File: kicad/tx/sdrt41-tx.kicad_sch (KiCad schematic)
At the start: 84 parts, among them J1 I, J2 Q, J3 Conn_01x05_Male, J4 TX, J5 Clock, J6 12V, Q1 2N3904_SOT23, T1 Transformer_1P_SS, U1 LM1117-3.3, U2 MC33078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

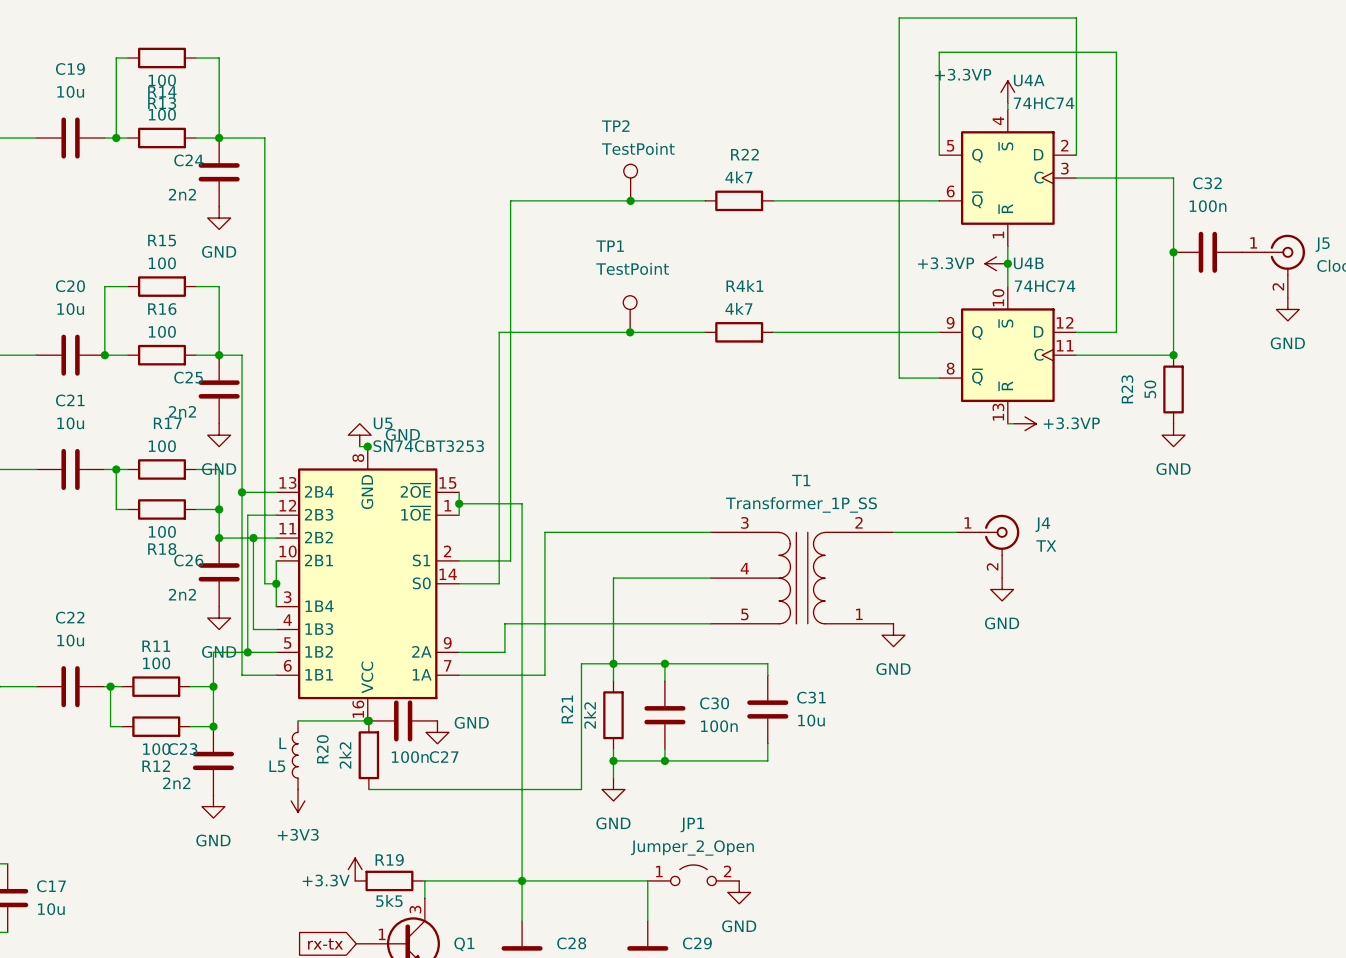
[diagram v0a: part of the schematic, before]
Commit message: Update TX capacitors
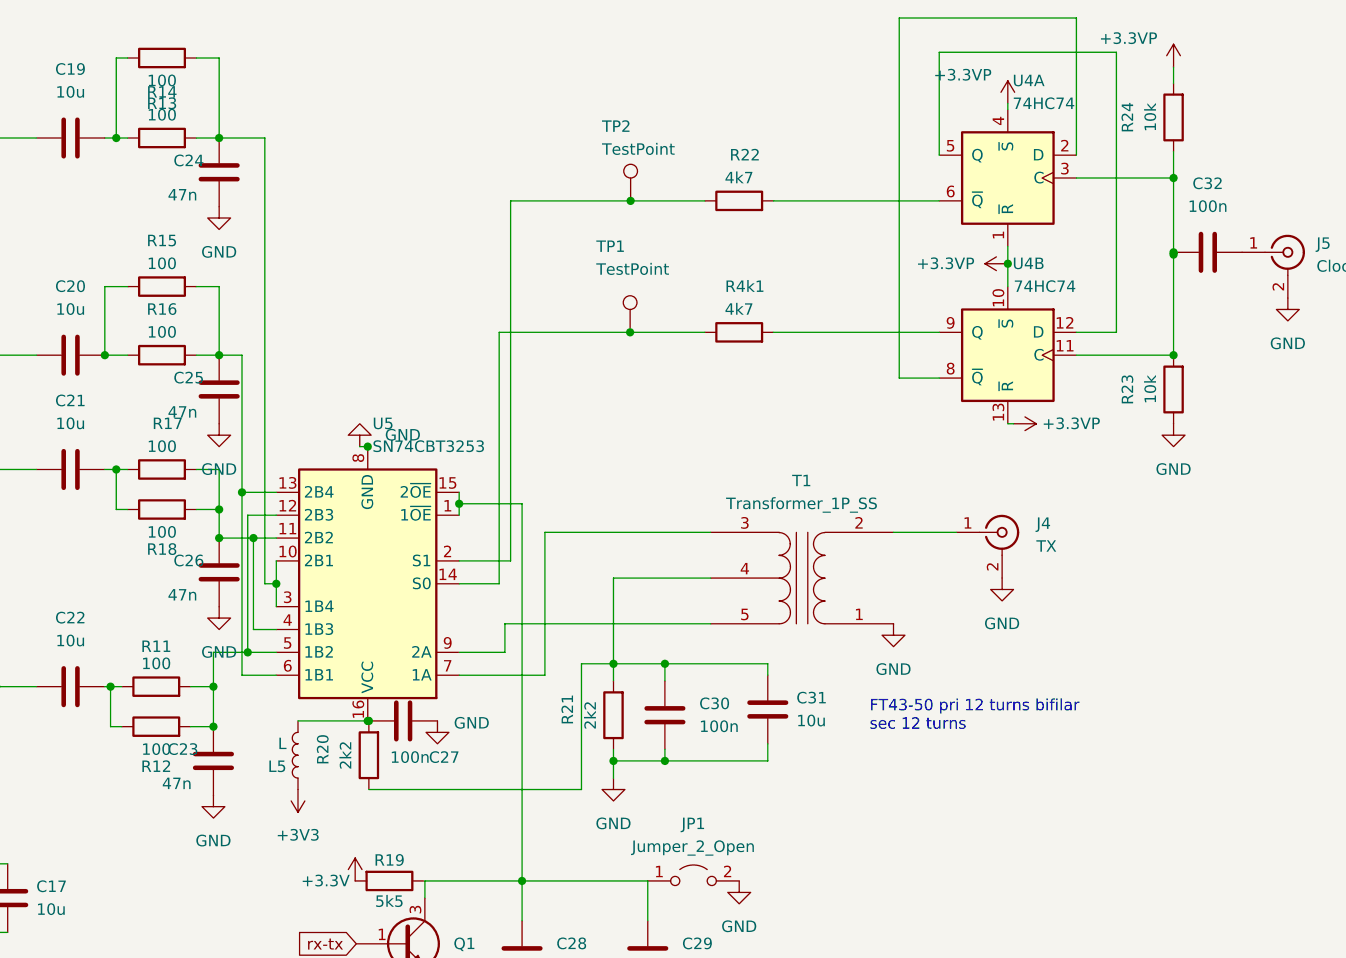
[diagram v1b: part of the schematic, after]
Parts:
- added R24: 10k, Resistor_SMD:R_0805_2012Metric, symbol Device:R
- C23, C24, C25, C26: value 2n2 -> 47n
- R23: value 50 -> 10k
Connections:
- net +3.3VP: now also R24.2
- net at C32.1, R23.2, U4.11 (C)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: now also R24.1
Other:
- note added: "FT43-50 pri 12 turns bifilar sec 12 turns"
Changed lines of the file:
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@@
   (junction (at 73.025 86.995) (diameter 0) (color 0 0 0 0)
   )
+  (junction (at 237.49 49.784) (diameter 0) (color 0 0 0 0)
+  )
   (junction (at 120.015 73.66) (diameter 0) (color 0 0 0 0)
   )
@@
   (junction (at 237.49 60.96) (diameter 0) (color 0 0 0 0)
   )
+  (junction (at 237.49 41.275) (diameter 0) (color 0 0 0 0)
+  )
   (junction (at 73.025 95.25) (diameter 0) (color 0 0 0 0)
   )
@@
     (stroke (width 0) (type default) (color 0 0 0 0))
   )
-  (wire (pts (xy 237.49 49.53) (xy 237.49 60.96))
+  (wire (pts (xy 237.49 49.53) (xy 237.49 49.784))
     (stroke (width 0) (type default) (color 0 0 0 0))
   )
@@
     (stroke (width 0) (type default) (color 0 0 0 0))
   )
+  (wire (pts (xy 237.49 49.784) (xy 237.49 60.96))
+    (stroke (width 0) (type default) (color 0 0 0 0))
+  )
   (wire (pts (xy 180.975 97.155) (xy 180.975 95.25))
     (stroke (width 0) (type default) (color 0 0 0 0))
@@
     (stroke (width 0) (type default) (color 0 0 0 0))
   )
+  (wire (pts (xy 237.49 41.275) (xy 237.49 49.53))
+    (stroke (width 0) (type default) (color 0 0 0 0))
+  )
   (wire (pts (xy 131.445 73.66) (xy 131.445 78.105))
     (stroke (width 0) (type default) (color 0 0 0 0))
@@
     (stroke (width 0) (type default) (color 0 0 0 0))
   )
+  (wire (pts (xy 237.49 30.734) (xy 237.49 28.956))
+    (stroke (width 0) (type default) (color 0 0 0 0))
+  )
   (wire (pts (xy 120.015 73.66) (xy 121.285 73.66))
     (stroke (width 0) (type default) (color 0 0 0 0))
@@
     (stroke (width 0) (type default) (color 0 0 0 0))
   )
-  (wire (pts (xy 237.49 41.275) (xy 237.49 49.53))
+  (wire (pts (xy 237.49 38.354) (xy 237.49 41.275))
     (stroke (width 0) (type default) (color 0 0 0 0))
   )
@@
     (stroke (width 0) (type default) (color 0 0 0 0))
   )
+  (wire (pts (xy 237.49 49.784) (xy 237.744 49.784))
+    (stroke (width 0) (type default) (color 0 0 0 0))
+  )
   (wire (pts (xy 180.975 104.775) (xy 180.975 106.045))
     (stroke (width 0) (type default) (color 0 0 0 0))
@@
     (stroke (width 0) (type default) (color 0 0 0 0))
   )
+  (text "FT43-50 pri 12 turns bifilar \nsec 12 turns" (at 203.708 102.87 0)
+    (effects (font (size 1.27 1.27)) (justify left bottom))
+  )
   (global_label "rx-tx" (shape input) (at 29.845 167.64 180) (fields_autoplaced)
     (effects (font (size 1.27 1.27)) (justify right))
@@
       (effects (font (size 1.27 1.27)) hide)
     )
+    (pin "1")
+    (pin "2")
+    (pin "3")
     (pin "5")
     (pin "6")
     (pin "7")
+    (pin "4")
+    (pin "8")
   )
   (symbol (lib_id "Connector:Screw_Terminal_01x02") (at 16.51 118.872 180) (unit 1)
@@
     (pin "2")
   )
+  (symbol (lib_id "power:+3.3VP") (at 237.49 28.956 0) (unit 1)
+    (in_bom yes) (on_board yes)
+    (property "Reference" "#PWR049" (id 0) (at 241.3 30.226 0)
+      (effects (font (size 1.27 1.27)) hide)
+    )
+    (property "Value" "+3.3VP" (id 1) (at 229.235 25.781 0)
+      (effects (font (size 1.27 1.27)) (justify left))
+    )
+    (property "Footprint" "" (id 2) (at 237.49 28.956 0)
+      (effects (font (size 1.27 1.27)) hide)
+    )
+    (property "Datasheet" "" (id 3) (at 237.49 28.956 0)
+      (effects (font (size 1.27 1.27)) hide)
+    )
+    (pin "1")
+  )
   (symbol (lib_id "power:GND") (at 36.195 100.33 0) (unit 1)
     (in_bom yes) (on_board yes)
@@
       (effects (font (size 1.27 1.27)) (justify right))
     )
-    (property "Value" "2n2" (id 1) (at 125.73 43.18 0)
+    (property "Value" "47n" (id 1) (at 125.73 43.18 0)
       (effects (font (size 1.27 1.27)) (justify right))
     )
@@
       (effects (font (size 1.27 1.27)) hide)
     )
+    (pin "1")
+    (pin "2")
+    (pin "3")
+    (pin "5")
+    (pin "6")
+    (pin "7")
     (pin "4")
     (pin "8")
@@
     (pin "5")
     (pin "6")
+    (pin "10")
+    (pin "11")
+    (pin "12")
+    (pin "13")
+    (pin "8")
+    (pin "9")
+    (pin "14")
+    (pin "7")
   )
   (symbol (lib_id "Analog_Switch:SN74CBT3253") (at 147.955 86.36 180) (unit 1)
@@
       (effects (font (size 1.27 1.27)) (justify right))
     )
-    (property "Value" "2n2" (id 1) (at 125.095 108.585 0)
+    (property "Value" "47n" (id 1) (at 125.095 108.585 0)
       (effects (font (size 1.27 1.27)) (justify right))
     )
@@
       (effects (font (size 1.27 1.27)) hide)
     )
+    (pin "1")
+    (pin "2")
+    (pin "3")
     (pin "5")
     (pin "6")
     (pin "7")
+    (pin "4")
+    (pin "8")
   )
   (symbol (lib_id "power:GND") (at 250.19 54.61 0) (mirror y) (unit 1)
@@
     (in_bom yes) (on_board yes)
     (property "Reference" "R23" (id 0) (at 232.41 64.77 90))
-    (property "Value" "50" (id 1) (at 234.95 64.77 90))
+    (property "Value" "10k" (id 1) (at 234.95 64.77 90))
     (property "Footprint" "Resistor_SMD:R_0805_2012Metric" (id 2) (at 239.268 64.77 90)
       (effects (font (size 1.27 1.27)) hide)
@@
     (pin "2")
   )
+  (symbol (lib_id "Device:R") (at 237.49 34.544 180) (unit 1)
+    (in_bom yes) (on_board yes)
+    (property "Reference" "R24" (id 0) (at 232.41 34.544 90))
+    (property "Value" "10k" (id 1) (at 234.95 34.544 90))
+    (property "Footprint" "Resistor_SMD:R_0805_2012Metric" (id 2) (at 239.268 34.544 90)
+      (effects (font (size 1.27 1.27)) hide)
+    )
+    (property "Datasheet" "~" (id 3) (at 237.49 34.544 0)
+      (effects (font (size 1.27 1.27)) hide)
+    )
+    (pin "1")
+    (pin "2")
+  )
   (symbol (lib_id "power:GND") (at 76.2 184.15 0) (unit 1)
     (in_bom yes) (on_board yes) (fields_autoplaced)
@@
       (effects (font (size 1.27 1.27)) hide)
     )
+    (pin "1")
+    (pin "2")
+    (pin "3")
+    (pin "4")
+    (pin "5")
+    (pin "6")
     (pin "10")
     (pin "11")
@@
     (pin "8")
     (pin "9")
+    (pin "14")
+    (pin "7")
   )
   (symbol (lib_id "power:GND") (at 179.07 131.445 0) (unit 1)
@@
       (effects (font (size 1.27 1.27)) (justify right))
     )
-    (property "Value" "2n2" (id 1) (at 125.73 67.31 0)
+    (property "Value" "47n" (id 1) (at 125.73 67.31 0)
       (effects (font (size 1.27 1.27)) (justify right))
     )
@@
     (pin "2")
     (pin "3")
+    (pin "5")
+    (pin "6")
+    (pin "7")
+    (pin "4")
+    (pin "8")
   )
   (symbol (lib_id "Device:C_Polarized") (at 58.547 142.748 0) (unit 1)
@@
       (effects (font (size 1.27 1.27)) (justify right))
     )
-    (property "Value" "2n2" (id 1) (at 125.73 87.63 0)
+    (property "Value" "47n" (id 1) (at 125.73 87.63 0)
       (effects (font (size 1.27 1.27)) (justify right))
     )
@@
       (effects (font (size 1.27 1.27)) hide)
     )
+    (pin "1")
+    (pin "2")
+    (pin "3")
+    (pin "4")
+    (pin "5")
+    (pin "6")
+    (pin "10")
+    (pin "11")
+    (pin "12")
+    (pin "13")
+    (pin "8")
+    (pin "9")
     (pin "14")
     (pin "7")
@@
       (effects (font (size 1.27 1.27)) hide)
     )
+    (pin "1")
+    (pin "2")
+    (pin "3")
+    (pin "5")
+    (pin "6")
+    (pin "7")
     (pin "4")
     (pin "8")
@@
     (pin "2")
     (pin "3")
+    (pin "5")
+    (pin "6")
+    (pin "7")
+    (pin "4")
+    (pin "8")
   )
   (symbol (lib_id "Device:L") (at 140.208 105.41 180) (unit 1)
@@
       (reference "#PWR048") (unit 1) (value "GND") (footprint "")
     )
+    (path "/1e0f91d5-660c-4fae-98b8-ab7f97c805f0"
+      (reference "#PWR049") (unit 1) (value "+3.3VP") (footprint "")
+    )
     (path "/7020aaf2-fa75-421e-82b9-e4517963d570"
       (reference "C1") (unit 1) (value "100u") (footprint "Capacitor_THT:C_Radial_D5.0mm_H7.0mm_P2.00mm")
@@
     )
     (path "/433ab9a2-9c06-417b-adc2-ea3da36a7a71"
-      (reference "C23") (unit 1) (value "2n2") (footprint "Capacitor_SMD:C_0805_2012Metric")
+      (reference "C23") (unit 1) (value "47n") (footprint "Capacitor_SMD:C_0805_2012Metric")
     )
     (path "/243e1090-cd87-4cc9-9be4-1f65c7892f7e"
-      (reference "C24") (unit 1) (value "2n2") (footprint "Capacitor_SMD:C_0805_2012Metric")
+      (reference "C24") (unit 1) (value "47n") (footprint "Capacitor_SMD:C_0805_2012Metric")
     )
     (path "/9a3166ca-c8ff-4512-842e-67fa90d0424d"
-      (reference "C25") (unit 1) (value "2n2") (footprint "Capacitor_SMD:C_0805_2012Metric")
+      (reference "C25") (unit 1) (value "47n") (footprint "Capacitor_SMD:C_0805_2012Metric")
     )
     (path "/d101552e-f79b-4cd8-a506-46d62076cd6b"
-      (reference "C26") (unit 1) (value "2n2") (footprint "Capacitor_SMD:C_0805_2012Metric")
+      (reference "C26") (unit 1) (value "47n") (footprint "Capacitor_SMD:C_0805_2012Metric")
     )
     (path "/63834c9d-d1be-43c1-96d7-ed507bfb48fc"
@@
     )
     (path "/52f95e37-03e2-4065-ab82-11166eaad9b2"
-      (reference "R23") (unit 1) (value "50") (footprint "Resistor_SMD:R_0805_2012Metric")
+      (reference "R23") (unit 1) (value "10k") (footprint "Resistor_SMD:R_0805_2012Metric")
+    )
+    (path "/5cedaf0c-1429-40ce-8043-2768e310e7ff"
+      (reference "R24") (unit 1) (value "10k") (footprint "Resistor_SMD:R_0805_2012Metric")
     )
     (path "/5e15ca0e-7d6c-44fa-b0d0-fa5e423ae194"

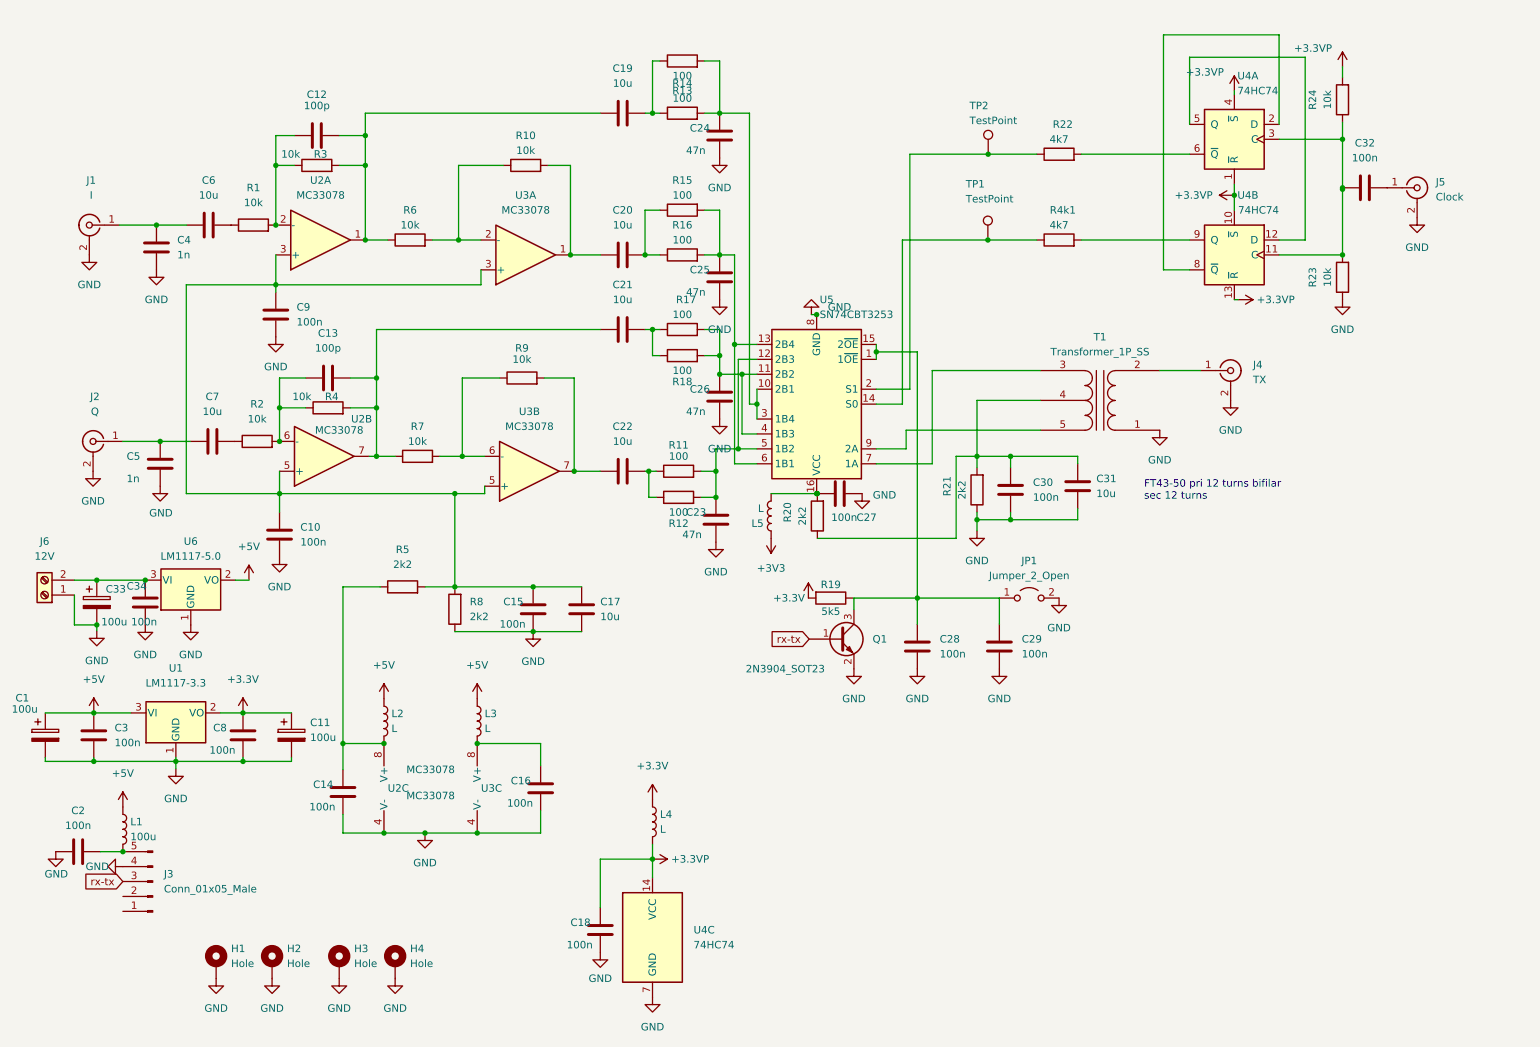
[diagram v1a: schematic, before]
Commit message: update gain and added differential  input setting
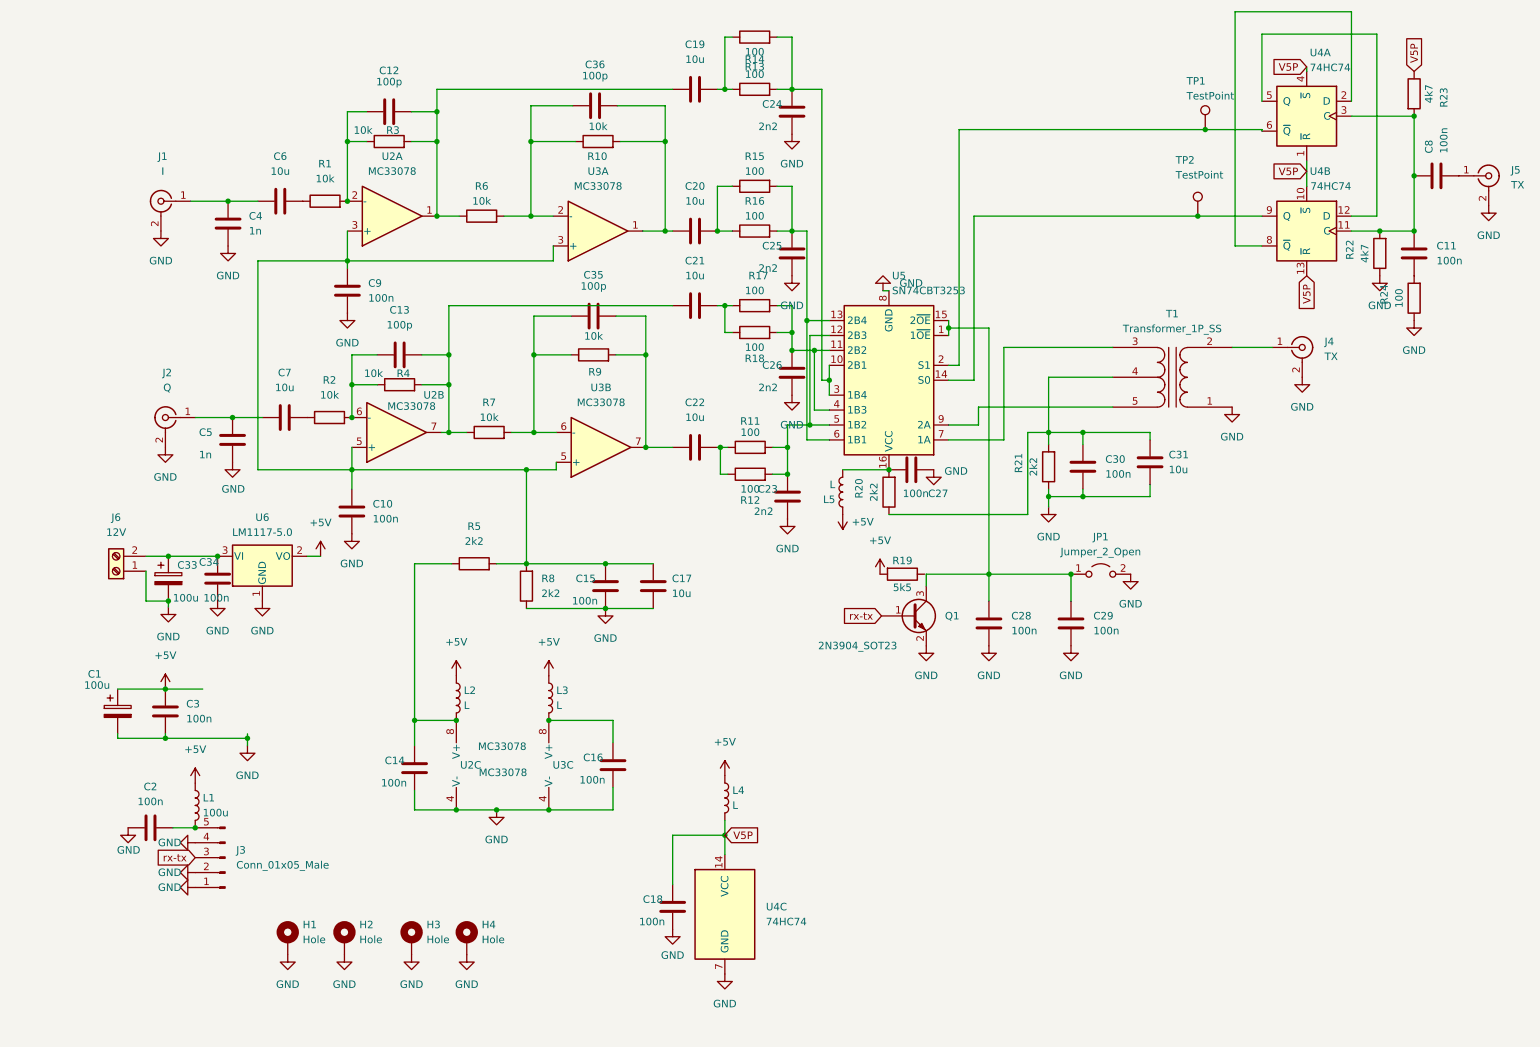
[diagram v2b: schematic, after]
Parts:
- removed C11: 100u, Capacitor_THT:C_Radial_D5.0mm_H7.0mm_P2.00mm, symbol Device:C_Polarized
- removed C32: 100n, Capacitor_SMD:C_0805_2012Metric, symbol Device:C
- removed R4k1: 4k7, Resistor_SMD:R_0805_2012Metric, symbol Device:R
- removed U1: LM1117-3.3, Package_TO_SOT_SMD:SOT-223-3_TabPin2, symbol Regulator_Linear:LM1117-3.3
- added C11: 100n, Capacitor_SMD:C_0805_2012Metric, symbol Device:C
- added C35, C36: 100p, Capacitor_SMD:C_0805_2012Metric, symbol Device:C
- C23, C24, C25, C26: value 47n -> 2n2
- J5: value Clock -> TX
- R23: value 10k -> 4k7
- R24: value 10k -> 100
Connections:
- net +5V: now also L4.1, L5.1, R19.2
- net GND: now also J3.1 (Pin_1), J3.2 (Pin_2), R22.1, R24.1; no longer C8.1, R23.1
- net at R10.1, R6.2, U3.2 (-): now also C36.2
- net at C20.1, R10.2, U3.1: now also C36.1
- net at R23.2, U4.11 (C), U4.3 (C): now also C8.2, R22.2, C11.2; no longer R24.1
- net at U4.6 (~{Q}): now also TP1.1, U5.2 (S1); no longer R22.2
- net at U5.14 (S0): now also TP2.1, U4.9 (Q); no longer TP1.1
- net at R7.2, R9.1, U3.6 (-): now also C35.2
- net at C22.1, R9.2, U3.7: now also C35.1
- net at J5.1 (In): now also C8.1
- net +3.3VP renamed V5P
- net V5P: now also R23.1; no longer R24.2
- removed net +3V3: C8.2, L4.1, L5.1, R19.2
- new net: C11.1, R24.2
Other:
- note removed: "FT43-50 pri 12 turns bifilar sec 12 turns"
- moved on the sheet: C1, C10, C12, C13, C14, C15, C16, C17, C18, C19, C2, C20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
